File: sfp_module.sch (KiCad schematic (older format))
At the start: 13 parts, among them J201 SFP

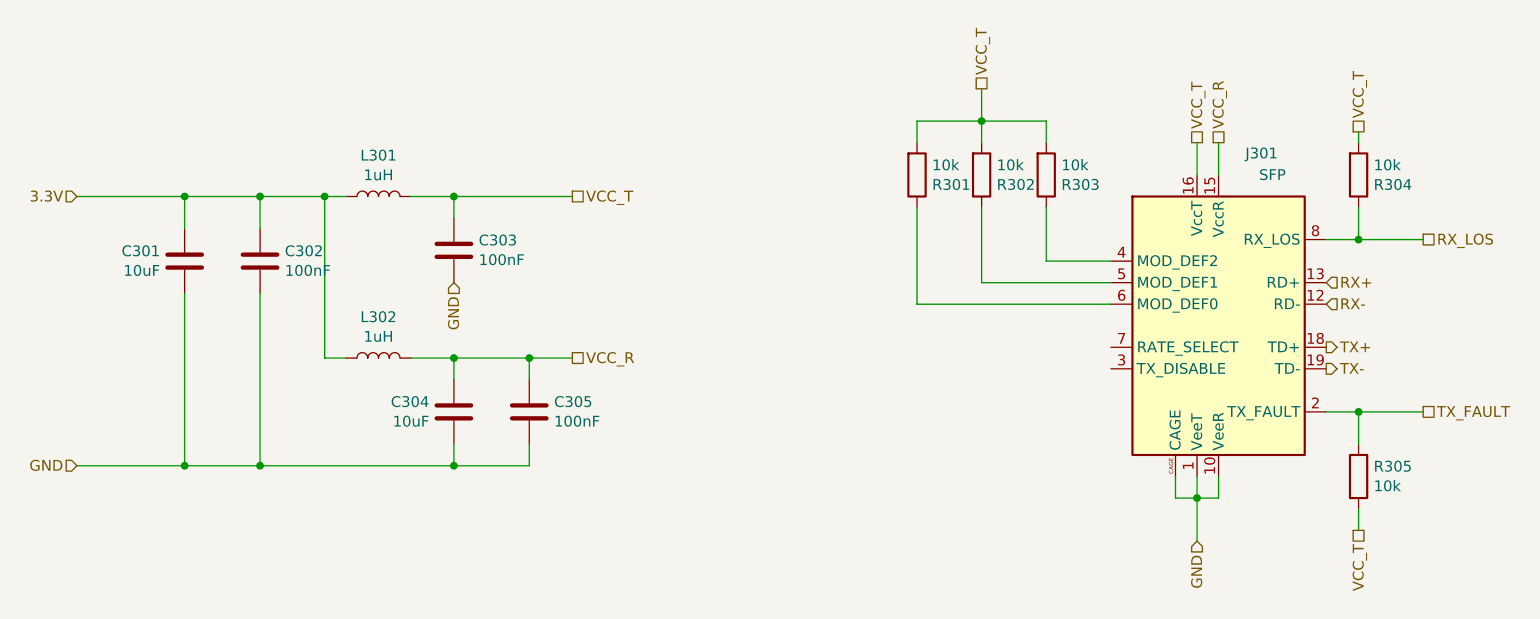
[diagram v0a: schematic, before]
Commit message: fix unconnected tx disable pin
Signed-off-by: Thomas Schmid <tom@binary-kitchen.de>
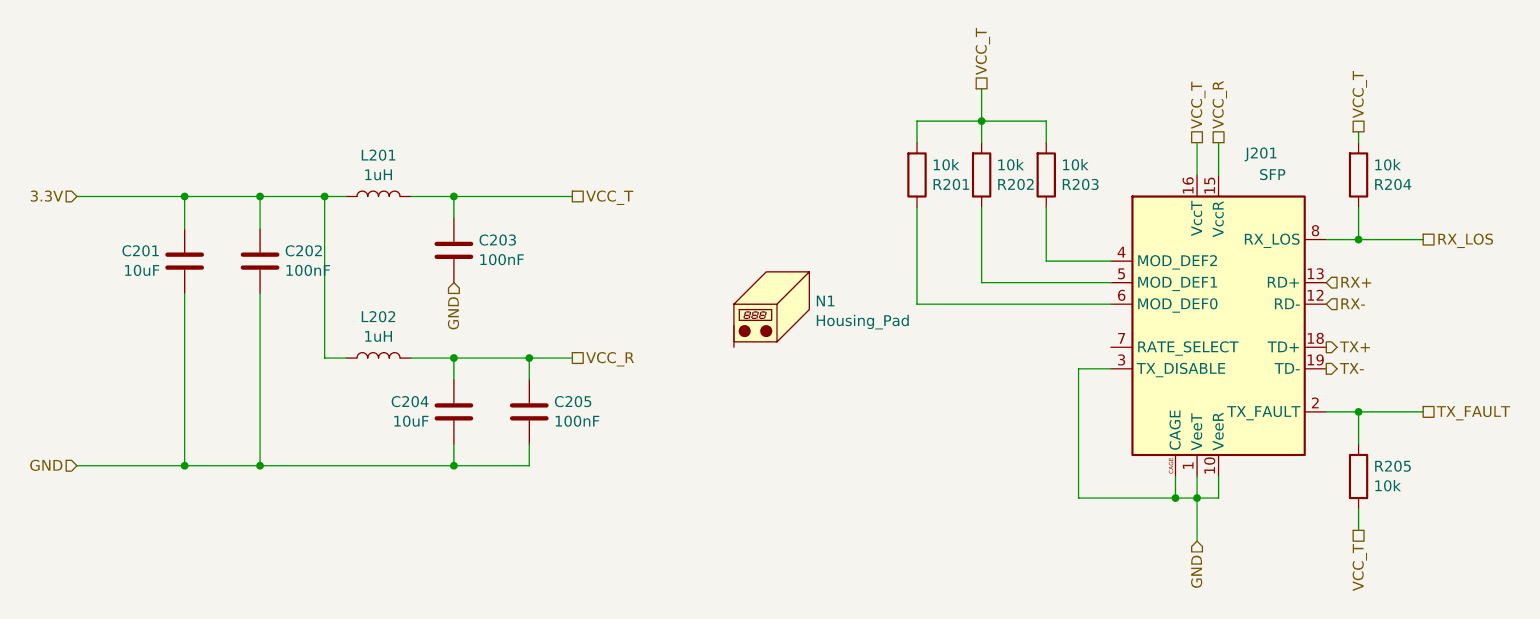
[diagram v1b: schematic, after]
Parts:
- added N1: Housing_Pad, symbol Mechanical:Housing_Pad
- C201, C204: Mouser Link (none) -> https://www.mouser.de/ProductDetail/Samsung-Electro-Mechani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; Mouser Part Number (none) -> 187-CL21A106KQFNNNG; Part Number (none) -> CL21A106KQFNNNG
- C202, C203, C205: Mouser Link (none) -> https://www.mouser.de/ProductDetail/AVX/06033C104KAT4A?qs=8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; Mouser Part Number (none) -> 581-06033C104KAT4A; Part Number (none) -> 06033C104KAT4A
- J201: Mouser Link (none) -> https://www.mouser.de/ProductDetail/Molex/74441-0001?qs=%2F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; Mouser Part Number (none) -> 538-74441-0001; Part Number (none) -> 74441-0001
- L201, L202: Mouser Link (none) -> https://www.mouser.de/ProductDetail/Taiyo-Yuden/MCKK2012T1R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; Mouser Part Number (none) -> 963-MCKK2012T1R0M; Part Number (none) -> MCKK2012T1R0M
- R201, R202, R203, R204, R205: Mouser Link (none) -> https://www.mouser.de/ProductDetail/Welwyn-Components-TT-El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; Mouser Part Number (none) -> 756-WCR0603-10KFA; Part Number (none) -> WCR0603-10KFA
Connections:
- net GND: now also J201.3 (TX_DISABLE)
